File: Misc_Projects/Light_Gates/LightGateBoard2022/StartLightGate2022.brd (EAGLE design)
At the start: 38.1 x 47.9 mm, 6 parts

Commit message: Light Gate Updates
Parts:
- removed IC1: (no value), GTOR - Active Components:TO-220
- removed X1: (no value), GTOR - Microfit Connector:43045-0600
- added IC2: (no value), GTOR - Active Components:TO-220-H
- added JP1: (no value), GTOR - Connectors:1X06
- moved R1 20.1 mm to (39.4, 41.9)
- moved R2 19.4 mm to (43.2, 41.9)
- moved X2 14.0 mm to (5.08, 26.7)
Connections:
- net +3V3: now also JP1.6; no longer X1.P$6
- net +5V: now also IC2.3; no longer IC1.3
- net GND: now also IC2.2, JP1.5; no longer IC1.2, X1.P$5
- net INT: now also JP1.1; no longer X1.P$1
- net SCL: now also JP1.3; no longer X1.P$3
- net SDA: now also JP1.4; no longer X1.P$4
- net SHUT: now also JP1.2; no longer X1.P$2
- net VCC: now also IC2.1; no longer IC1.1
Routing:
- net +3V3: track 39.5 -> 81.9 mm
- net SDA: track 19.1 -> 49.8 mm
- net +5V: track 30.8 -> 56.3 mm
- net VCC: track 15.7 -> 40.1 mm
- net INPUT: track 46.2 -> 28.2 mm
- net SHUT: track 49.2 -> 36.4 mm
- net INT: track 24.7 -> 32.3 mm
- net SCL: track 42.9 -> 47.5 mm
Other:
- board size 38.1 x 47.9 mm -> 57.1 x 49.5 mm

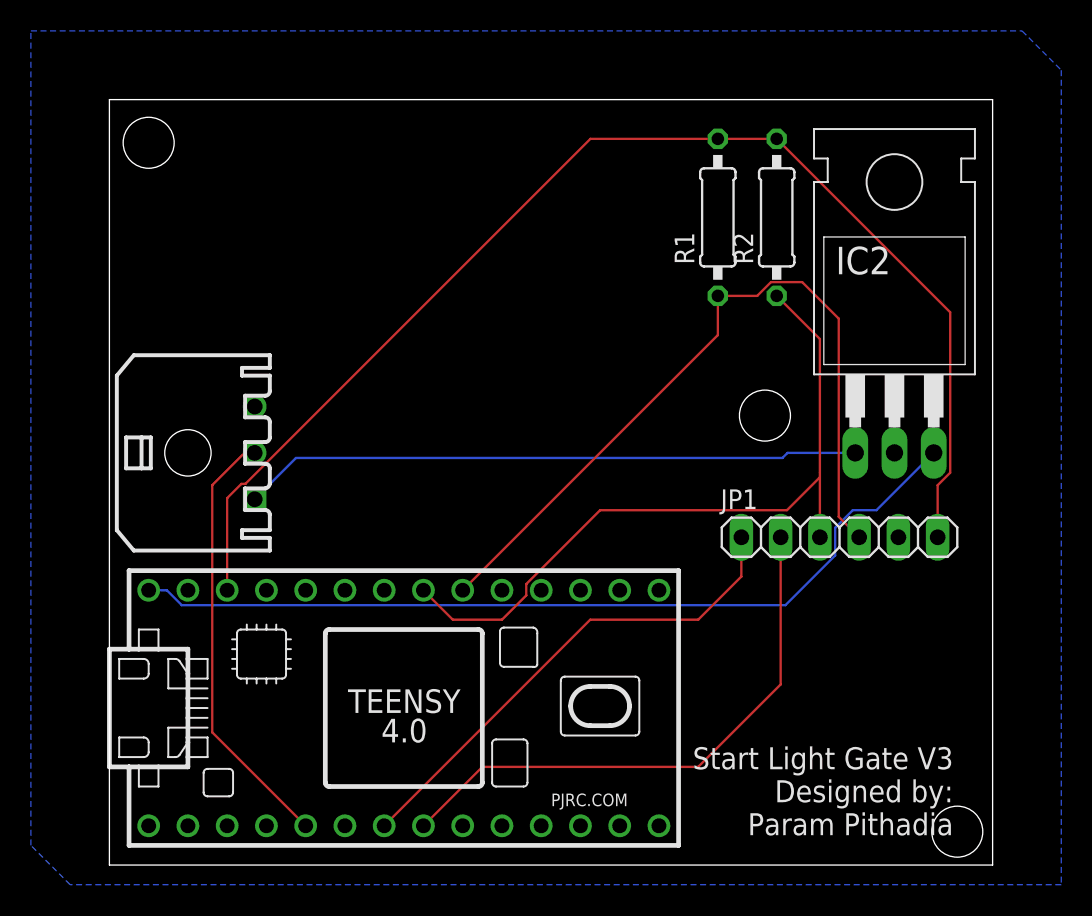
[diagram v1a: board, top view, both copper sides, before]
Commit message: Fixeed light gate start board
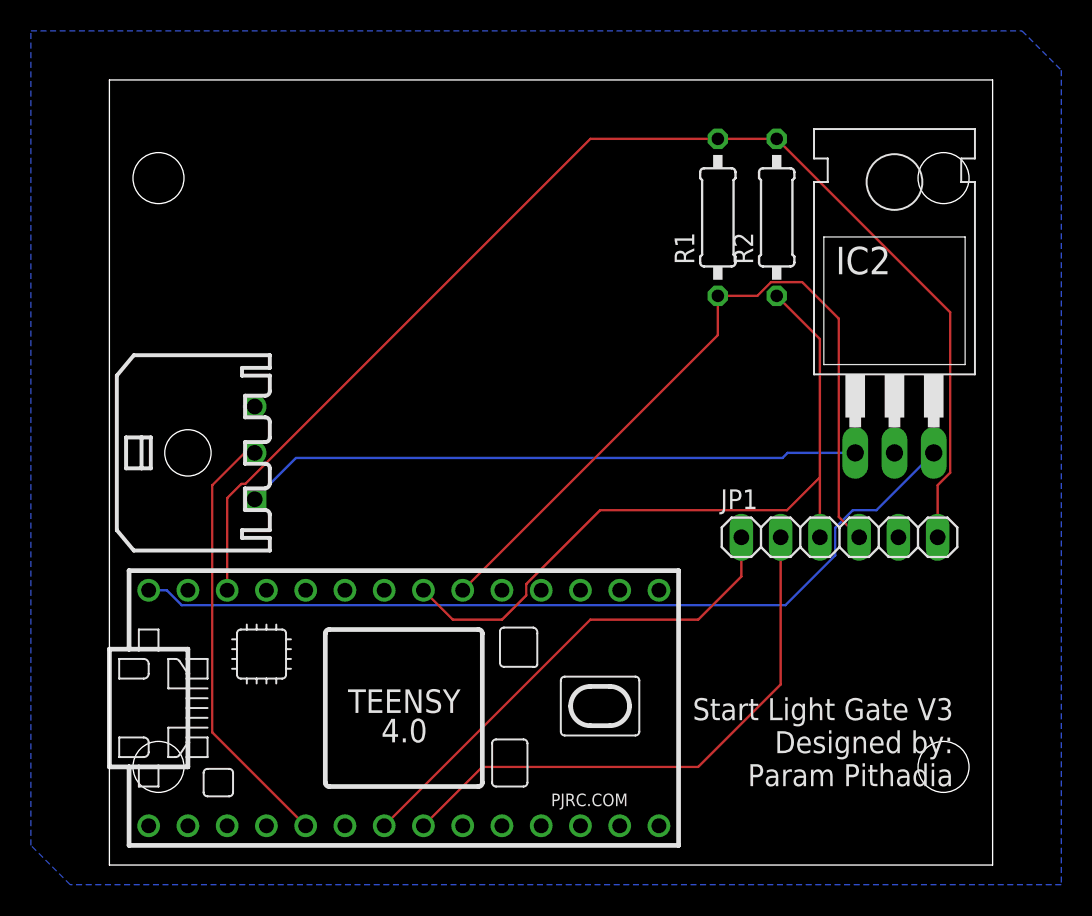
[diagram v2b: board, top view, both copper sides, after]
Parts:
- R1, R2: value (none) -> 10k
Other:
- board size 57.1 x 49.5 mm -> 57.1 x 50.8 mm
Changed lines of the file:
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@@
 <plain>
 <wire x1="0" y1="0" x2="57.15" y2="0" width="0" layer="20"/>
-<wire x1="57.15" y1="0" x2="57.15" y2="49.53" width="0" layer="20"/>
-<wire x1="57.15" y1="49.53" x2="0" y2="49.53" width="0" layer="20"/>
-<wire x1="0" y1="49.53" x2="0" y2="0" width="0" layer="20"/>
-<text x="54.61" y="7.62" size="1.4224" layer="25" rot="R180">Start Light Gate V3
+<wire x1="57.15" y1="0" x2="57.15" y2="50.8" width="0" layer="20"/>
+<wire x1="57.15" y1="50.8" x2="0" y2="50.8" width="0" layer="20"/>
+<wire x1="0" y1="50.8" x2="0" y2="0" width="0" layer="20"/>
+<text x="54.61" y="10.795" size="1.4224" layer="25" rot="R180">Start Light Gate V3
 Designed by:
 Param Pithadia</text>
-<hole x="2.54" y="46.736" drill="3.3"/>
-<hole x="42.418" y="29.083" drill="3.3"/>
-<hole x="54.864" y="2.159" drill="3.3"/>
+<hole x="3.175" y="6.35" drill="3.3"/>
+<hole x="53.975" y="44.45" drill="3.3"/>
+<hole x="53.975" y="6.35" drill="3.3"/>
+<hole x="3.175" y="44.45" drill="3.3"/>
 </plain>
 <attributes>
@@
 <element name="U$1" library="GTOR - Microcontroller" package="TEENSY_4.0_SIMPLE" value="TEENSY_4.0_SIMPLE" x="19.05" y="10.16" smashed="yes"/>
 <element name="X2" library="GTOR - Microfit Connector" package="43650-0300" value="" x="5.08" y="26.67" smashed="yes" rot="R270"/>
-<element name="R1" library="GTOR - Passive Components" package="1/4W-0.4" package3d_urn="urn:adsk.eagle:package:23491/2" value="" x="39.37" y="41.91" smashed="yes" rot="R90">
+<element name="R1" library="GTOR - Passive Components" package="1/4W-0.4" package3d_urn="urn:adsk.eagle:package:23491/2" value="10k" x="39.37" y="41.91" smashed="yes" rot="R90">
 <attribute name="NAME" x="37.846" y="38.862" size="1.27" layer="25" ratio="10" rot="R90"/>
 <attribute name="POPULARITY" value="36" x="39.37" y="41.91" size="1.4224" layer="27" rot="R90" display="off"/>
@@
 <attribute name="VALUE" x="40.005" y="39.6494" size="1.27" layer="27" ratio="10" rot="R90"/>
 </element>
-<element name="R2" library="GTOR - Passive Components" package="1/4W-0.4" package3d_urn="urn:adsk.eagle:package:23491/2" value="" x="43.18" y="41.91" smashed="yes" rot="R90">
+<element name="R2" library="GTOR - Passive Components" package="1/4W-0.4" package3d_urn="urn:adsk.eagle:package:23491/2" value="10k" x="43.18" y="41.91" smashed="yes" rot="R90">
 <attribute name="NAME" x="41.656" y="38.862" size="1.27" layer="25" ratio="10" rot="R90"/>
 <attribute name="POPULARITY" value="36" x="43.18" y="41.91" size="1.4224" layer="27" rot="R90" display="off"/>
